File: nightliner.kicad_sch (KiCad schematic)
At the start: 84 parts, among them J1 TYPE-C-31-M-12, J2 Battery, J3 Battery, P1 ISP_Prog, SW1 pinky_top, SW10 inner_home, SW11 pinky_bottom, SW12 ring_bottom, SW13 middle_bottom, SW14 index_bottom, SW15 inner_bottom, SW16 outer_top, SW17 outer_home, SW18 near_thumb, SW19 home_thumb, SW2 ring_top, SW20 far_thumb, SW21 ON_OFF, SW22 RESET, SW3 middle_top, SW4 index_top, SW5 inner_top, SW6 pinky_home, SW7 ring_home, SW8 middle_home, SW9 index_home, U1 holyiot-18010, U2 TVS2200DRV, U3 USBLC6-2SC6, U4 BQ24075RGT, U5 XC6220B331MR

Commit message: feat: move all outlines to KiCAD, update footprints
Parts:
- SW1, SW10, SW11, SW12, SW13, SW14, SW15, SW16, SW17, SW18, SW19, SW2, SW20, SW3, SW4, SW5, SW6, SW7, SW8, SW9: footprint kleeb_choc:pg1350-H -> miro_keyboard:Kailh_Choc_CPG135001D02_Hotswap
- U1: footprint miro_keyboard:holyiot-18010 -> miro_keyboard:HOLYIOT-18010-UndersidePins-SMD
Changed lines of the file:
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@@
       (effects (font (size 1.27 1.27)) hide)
     )
-    (property "Footprint" "kleeb_choc:pg1350-H" (at 204.47 64.77 0)
+    (property "Footprint" "miro_keyboard:Kailh_Choc_CPG135001D02_Hotswap" (at 204.47 64.77 0)
       (effects (font (size 1.27 1.27)) hide)
     )
@@
       (effects (font (size 1.27 1.27)) hide)
     )
-    (property "Footprint" "kleeb_choc:pg1350-H" (at 245.11 64.77 0)
+    (property "Footprint" "miro_keyboard:Kailh_Choc_CPG135001D02_Hotswap" (at 245.11 64.77 0)
       (effects (font (size 1.27 1.27)) hide)
     )
@@
       (effects (font (size 1.27 1.27)) hide)
     )
-    (property "Footprint" "kleeb_choc:pg1350-H" (at 204.47 49.53 0)
+    (property "Footprint" "miro_keyboard:Kailh_Choc_CPG135001D02_Hotswap" (at 204.47 49.53 0)
       (effects (font (size 1.27 1.27)) hide)
     )
@@
       (effects (font (size 1.27 1.27)) hide)
     )
-    (property "Footprint" "kleeb_choc:pg1350-H" (at 184.15 80.01 0)
+    (property "Footprint" "miro_keyboard:Kailh_Choc_CPG135001D02_Hotswap" (at 184.15 80.01 0)
       (effects (font (size 1.27 1.27)) hide)
     )
@@
       (effects (font (size 1.27 1.27)) hide)
     )
-    (property "Footprint" "kleeb_choc:pg1350-H" (at 204.47 80.01 0)
+    (property "Footprint" "miro_keyboard:Kailh_Choc_CPG135001D02_Hotswap" (at 204.47 80.01 0)
       (effects (font (size 1.27 1.27)) hide)
     )
@@
       (effects (font (size 1.27 1.27)) hide)
     )
-    (property "Footprint" "kleeb_choc:pg1350-H" (at 224.79 49.53 0)
+    (property "Footprint" "miro_keyboard:Kailh_Choc_CPG135001D02_Hotswap" (at 224.79 49.53 0)
       (effects (font (size 1.27 1.27)) hide)
     )
@@
       (effects (font (size 1.27 1.27)) hide)
     )
-    (property "Footprint" "kleeb_choc:pg1350-H" (at 224.79 80.01 0)
+    (property "Footprint" "miro_keyboard:Kailh_Choc_CPG135001D02_Hotswap" (at 224.79 80.01 0)
       (effects (font (size 1.27 1.27)) hide)
     )
@@
       (effects (font (size 1.27 1.27)))
     )
-    (property "Footprint" "miro_keyboard:holyiot-18010" (at 58.42 95.25 0)
+    (property "Footprint" "miro_keyboard:HOLYIOT-18010-UndersidePins-SMD" (at 58.42 95.25 0)
       (effects (font (size 1.27 1.27)) hide)
     )
@@
       (effects (font (size 1.27 1.27)) hide)
     )
-    (property "Footprint" "kleeb_choc:pg1350-H" (at 265.43 34.29 0)
+    (property "Footprint" "miro_keyboard:Kailh_Choc_CPG135001D02_Hotswap" (at 265.43 34.29 0)
       (effects (font (size 1.27 1.27)) hide)
     )
@@
       (effects (font (size 1.27 1.27)) hide)
     )
-    (property "Footprint" "kleeb_choc:pg1350-H" (at 224.79 64.77 0)
+    (property "Footprint" "miro_keyboard:Kailh_Choc_CPG135001D02_Hotswap" (at 224.79 64.77 0)
       (effects (font (size 1.27 1.27)) hide)
     )
@@
       (effects (font (size 1.27 1.27)) hide)
     )
-    (property "Footprint" "kleeb_choc:pg1350-H" (at 245.11 80.01 0)
+    (property "Footprint" "miro_keyboard:Kailh_Choc_CPG135001D02_Hotswap" (at 245.11 80.01 0)
       (effects (font (size 1.27 1.27)) hide)
     )
@@
       (effects (font (size 1.27 1.27)) hide)
     )
-    (property "Footprint" "kleeb_choc:pg1350-H" (at 224.79 34.29 0)
+    (property "Footprint" "miro_keyboard:Kailh_Choc_CPG135001D02_Hotswap" (at 224.79 34.29 0)
       (effects (font (size 1.27 1.27)) hide)
     )
@@
       (effects (font (size 1.27 1.27)) hide)
     )
-    (property "Footprint" "kleeb_choc:pg1350-H" (at 245.11 34.29 0)
+    (property "Footprint" "miro_keyboard:Kailh_Choc_CPG135001D02_Hotswap" (at 245.11 34.29 0)
       (effects (font (size 1.27 1.27)) hide)
     )
@@
       (effects (font (size 1.27 1.27)) hide)
     )
-    (property "Footprint" "kleeb_choc:pg1350-H" (at 245.11 49.53 0)
+    (property "Footprint" "miro_keyboard:Kailh_Choc_CPG135001D02_Hotswap" (at 245.11 49.53 0)
       (effects (font (size 1.27 1.27)) hide)
     )
@@
       (effects (font (size 1.27 1.27)) hide)
     )
-    (property "Footprint" "kleeb_choc:pg1350-H" (at 265.43 64.77 0)
+    (property "Footprint" "miro_keyboard:Kailh_Choc_CPG135001D02_Hotswap" (at 265.43 64.77 0)
       (effects (font (size 1.27 1.27)) hide)
     )
@@
       (effects (font (size 1.27 1.27)) hide)
     )
-    (property "Footprint" "kleeb_choc:pg1350-H" (at 204.47 34.29 0)
+    (property "Footprint" "miro_keyboard:Kailh_Choc_CPG135001D02_Hotswap" (at 204.47 34.29 0)
       (effects (font (size 1.27 1.27)) hide)
     )
@@
       (effects (font (size 1.27 1.27)) hide)
     )
-    (property "Footprint" "kleeb_choc:pg1350-H" (at 265.43 49.53 0)
+    (property "Footprint" "miro_keyboard:Kailh_Choc_CPG135001D02_Hotswap" (at 265.43 49.53 0)
       (effects (font (size 1.27 1.27)) hide)
     )
@@
       (effects (font (size 1.27 1.27)) hide)
     )
-    (property "Footprint" "kleeb_choc:pg1350-H" (at 184.15 64.77 0)
+    (property "Footprint" "miro_keyboard:Kailh_Choc_CPG135001D02_Hotswap" (at 184.15 64.77 0)
       (effects (font (size 1.27 1.27)) hide)
     )
@@
       (effects (font (size 1.27 1.27)) hide)
     )
-    (property "Footprint" "kleeb_choc:pg1350-H" (at 184.15 34.29 0)
+    (property "Footprint" "miro_keyboard:Kailh_Choc_CPG135001D02_Hotswap" (at 184.15 34.29 0)
       (effects (font (size 1.27 1.27)) hide)
     )
@@
       (effects (font (size 1.27 1.27)) hide)
     )
-    (property "Footprint" "kleeb_choc:pg1350-H" (at 265.43 80.01 0)
+    (property "Footprint" "miro_keyboard:Kailh_Choc_CPG135001D02_Hotswap" (at 265.43 80.01 0)
       (effects (font (size 1.27 1.27)) hide)
     )
@@
       (effects (font (size 1.27 1.27)) hide)
     )
-    (property "Footprint" "kleeb_choc:pg1350-H" (at 184.15 49.53 0)
-      (effects (font (size 1.27 1.27)) hide)
-    )
+    (property "Footprint" "miro_keyboard:Kailh_Choc_CPG135001D02_Hotswap" (at 184.15 49.53 0)
+      (effects (font (size 1.27 1.27)) hide)
+    )

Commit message: feat: case for the keyboard
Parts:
- H1: value MountingHole_M3 -> Standoff_6mm_M3; footprint MountingHole:MountingHole_6.4mm_M6 -> miro_keyboard:StandOff_6mm_M3
- H2, H3, H4, H5, H6, H7: footprint MountingHole:MountingHole_6.4mm_M6 -> miro_keyboard:StandOff_6mm_M3
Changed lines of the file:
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@@
       (effects (font (size 1.27 1.27)) (justify left) hide)
     )
-    (property "Footprint" "MountingHole:MountingHole_6.4mm_M6" (at 90.17 90.17 0)
+    (property "Footprint" "miro_keyboard:StandOff_6mm_M3" (at 90.17 90.17 0)
       (effects (font (size 1.27 1.27)) hide)
     )
@@
       (effects (font (size 1.27 1.27)) (justify left) hide)
     )
-    (property "Footprint" "MountingHole:MountingHole_6.4mm_M6" (at 90.17 83.82 0)
+    (property "Footprint" "miro_keyboard:StandOff_6mm_M3" (at 90.17 83.82 0)
       (effects (font (size 1.27 1.27)) hide)
     )
@@
       (effects (font (size 1.27 1.27)) (justify left))
     )
-    (property "Value" "MountingHole_M3" (at 73.66 81.28 0)
+    (property "Value" "Standoff_6mm_M3" (at 73.66 81.28 0)
       (effects (font (size 1.27 1.27)) (justify left) hide)
     )
-    (property "Footprint" "MountingHole:MountingHole_6.4mm_M6" (at 69.85 83.82 0)
+    (property "Footprint" "miro_keyboard:StandOff_6mm_M3" (at 69.85 83.82 0)
       (effects (font (size 1.27 1.27)) hide)
     )
@@
       (effects (font (size 1.27 1.27)) (justify left) hide)
     )
-    (property "Footprint" "MountingHole:MountingHole_6.4mm_M6" (at 100.33 83.82 0)
+    (property "Footprint" "miro_keyboard:StandOff_6mm_M3" (at 100.33 83.82 0)
       (effects (font (size 1.27 1.27)) hide)
     )
@@
       (effects (font (size 1.27 1.27)) (justify left) hide)
     )
-    (property "Footprint" "MountingHole:MountingHole_6.4mm_M6" (at 80.01 90.17 0)
+    (property "Footprint" "miro_keyboard:StandOff_6mm_M3" (at 80.01 90.17 0)
       (effects (font (size 1.27 1.27)) hide)
     )
@@
       (effects (font (size 1.27 1.27)) (justify left) hide)
     )
-    (property "Footprint" "MountingHole:MountingHole_6.4mm_M6" (at 69.85 90.17 0)
+    (property "Footprint" "miro_keyboard:StandOff_6mm_M3" (at 69.85 90.17 0)
       (effects (font (size 1.27 1.27)) hide)
     )
@@
       (effects (font (size 1.27 1.27)) (justify left) hide)
     )
-    (property "Footprint" "MountingHole:MountingHole_6.4mm_M6" (at 80.01 83.82 0)
-      (effects (font (size 1.27 1.27)) hide)
-    )
+    (property "Footprint" "miro_keyboard:StandOff_6mm_M3" (at 80.01 83.82 0)
+      (effects (font (size 1.27 1.27)) hide)
+    )

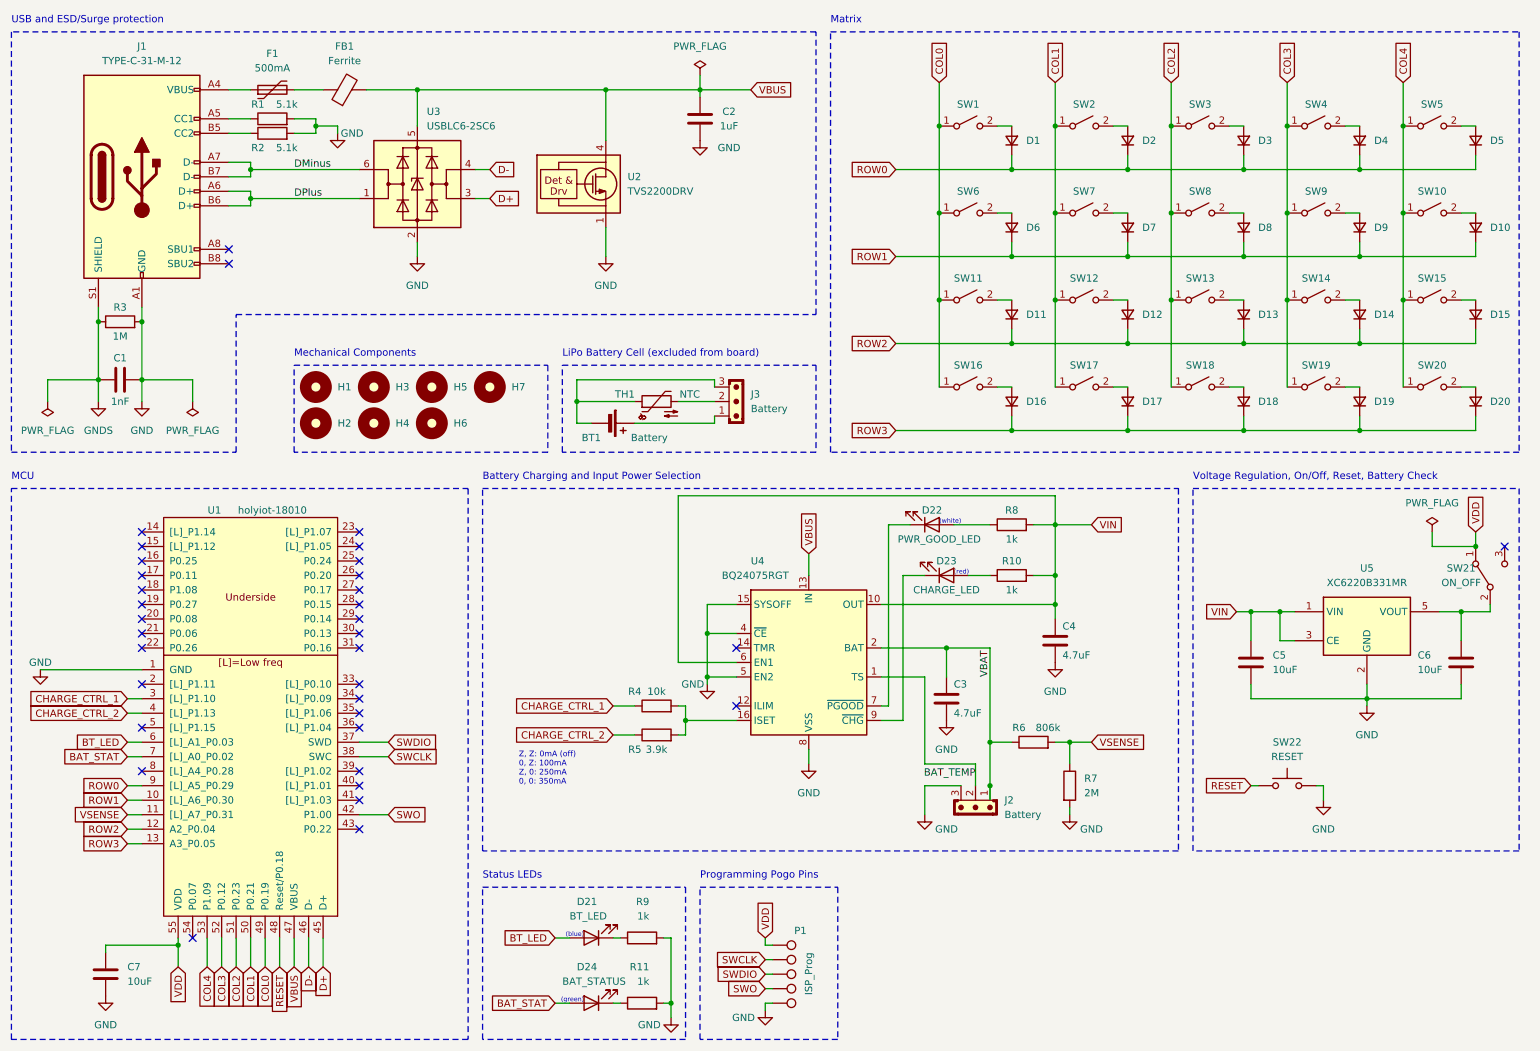
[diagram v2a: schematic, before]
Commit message: feat: add split pogo connector, reroute board
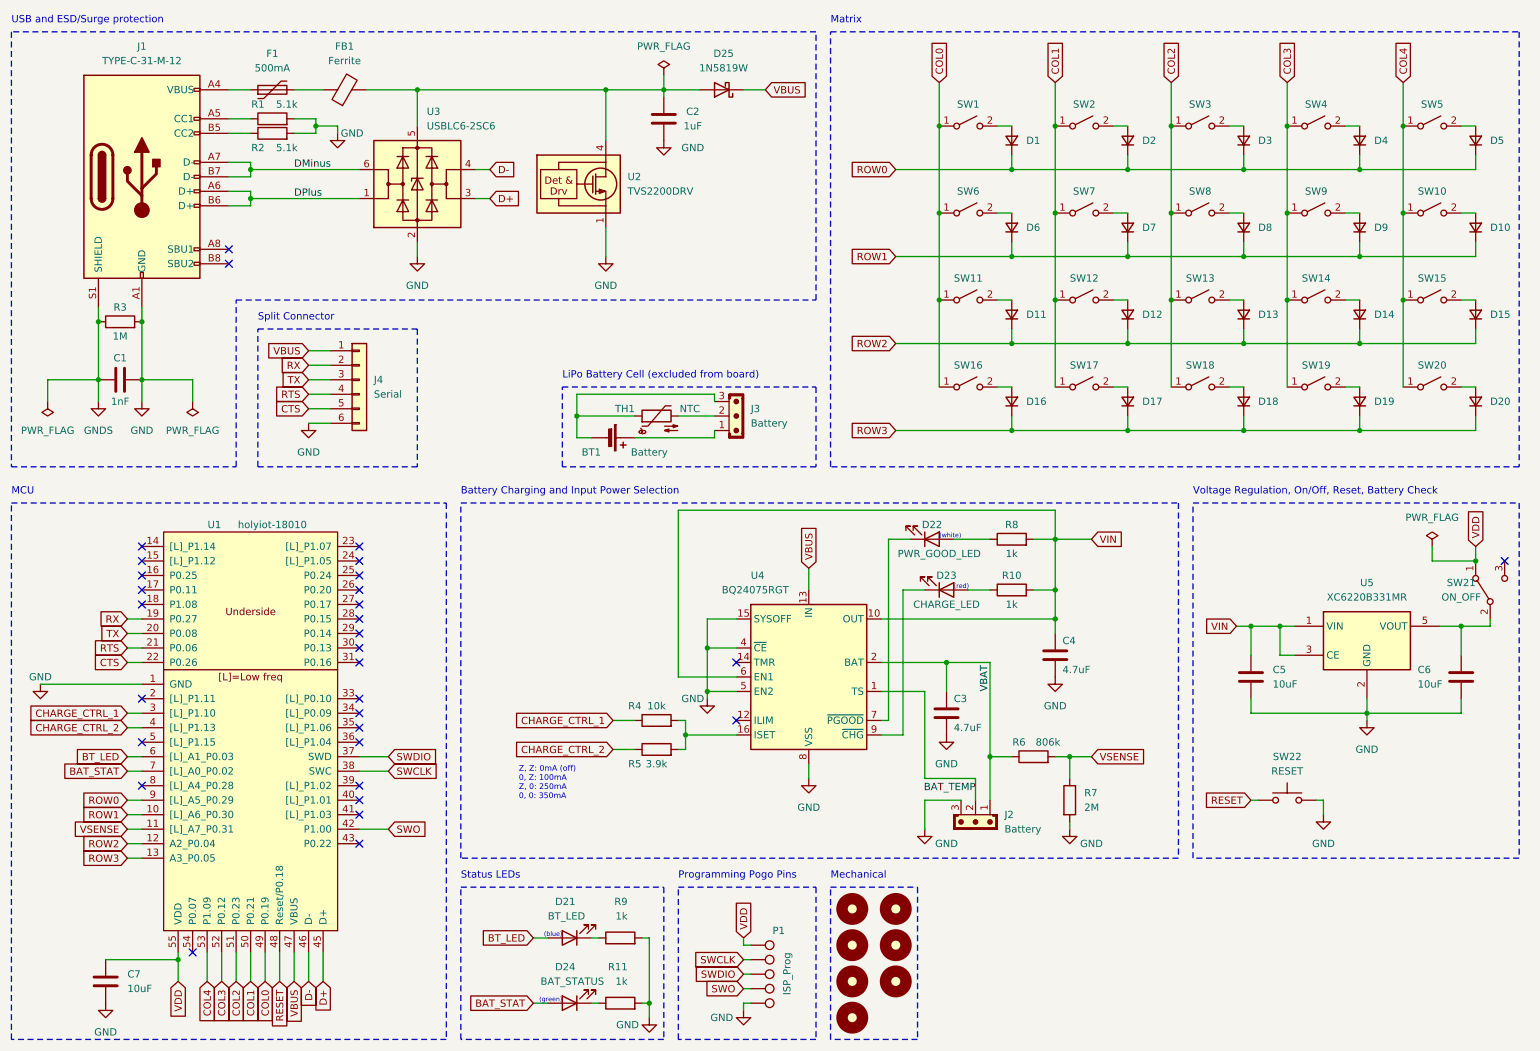
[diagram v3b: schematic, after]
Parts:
- added D25: 1N5819W, Diode_SMD:D_SOD-123, symbol Device:D_Schottky
- added J4: Serial, miro_keyboard:MagConn_6pin_left, symbol Connector_Generic:Conn_01x06
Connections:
- net GND: now also J4.6 (Pin_6)
- net VBUS: now also D25.1 (K), J4.1 (Pin_1); no longer C2.2, FB1.2, U2.4 (IN), U2.5 (IN), U2.6 (IN), U3.5 (VBUS)
- net RX: now reaches U1.19 (P0.27)
- net RX: now also J4.2 (Pin_2)
- net TX: now reaches U1.20 (P0.08)
- net TX: now also J4.3 (Pin_3)
- net RTS: now reaches U1.21 (P0.06)
- net RTS: now also J4.4 (Pin_4)
- net CTS: now reaches U1.22 (P0.26)
- net CTS: now also J4.5 (Pin_5)
- new net: C2.2, D25.2 (A), FB1.2, U2.4 (IN), U2.5 (IN), U2.6 (IN), U3.5 (VBUS)
- no-connect marks 35 -> 31
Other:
- note added: "Mechanical"
- note added: "Split Connector"
- note removed: "Mechanical Components"
- moved on the sheet: BT1, C2, C3, C4, C5, C6, C7, D21, D22, D23, D24, J2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
